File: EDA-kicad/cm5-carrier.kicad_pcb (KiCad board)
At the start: 2 copper layers, 82 x 154.8 mm, 94 parts, among them J1 SJ2-35894B-SMT-TR, J2 USBC-4-0-CX90MW9-24P1, J3 SIM-G85D1160022HHR, J4 FINGER, Q10 NMOS, Q3 NMOS, Q3_BAT1 NMOS, Q4 NMOS, Q4_BAT1 NMOS, Q5 NMOS, Q6 NMOS, Q7 NMOS, Q8 NMOS, Q9 NMOS, SW2 PROG, SW3 VOL-, SW4 VOL+, SW5 POW, SW6 CHP-041B, U1 EG25GGC-128-SGNS, U10 BAT-CONNECTOR-FLTS22WR00, U5 Flash-LED-Lumiled, U6 FPC15pin-1mm-pitch-F52Q-1A7H1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, U7 CODEC-TLV320AIC3204IRHBR, U8 DAC-TLV320DAC3100IRHBR, U9 GSM-GPS-EC25VFA-512-STD

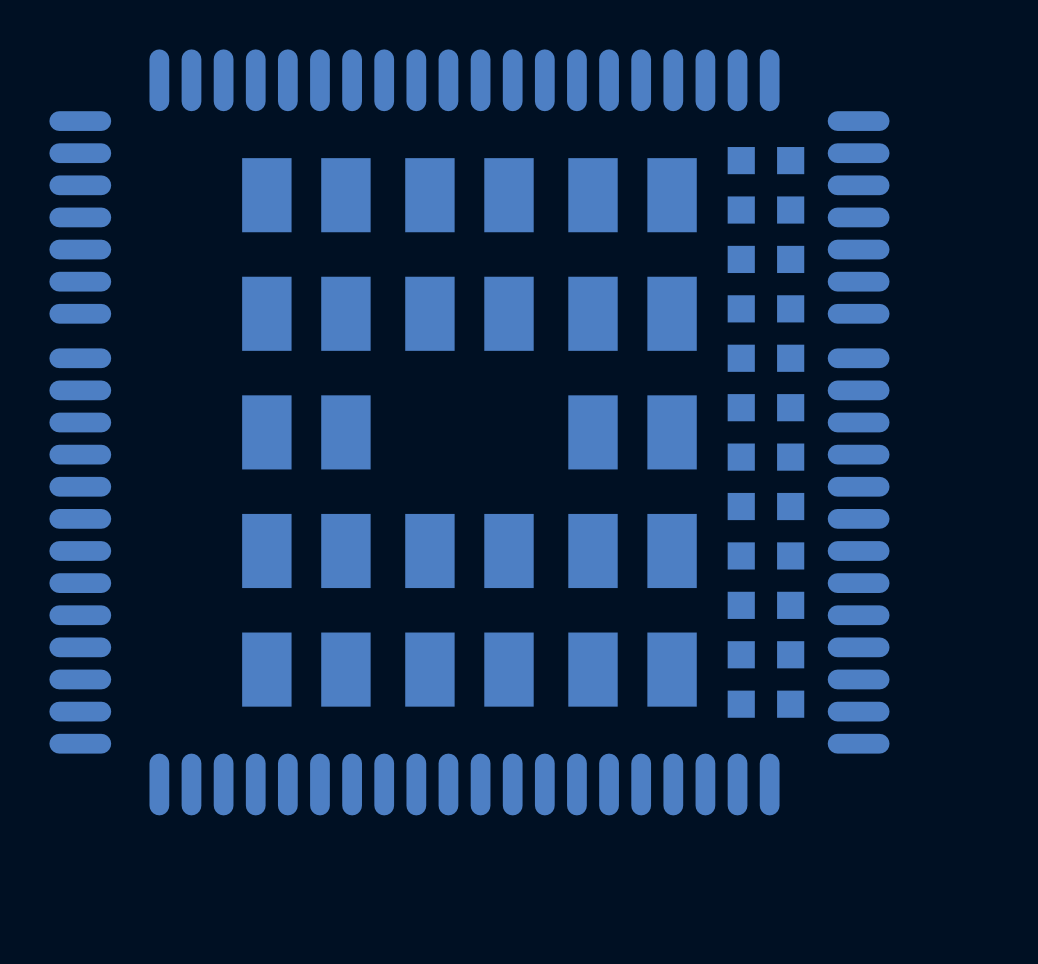
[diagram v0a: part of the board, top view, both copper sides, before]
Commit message: delete old ec25 footprint
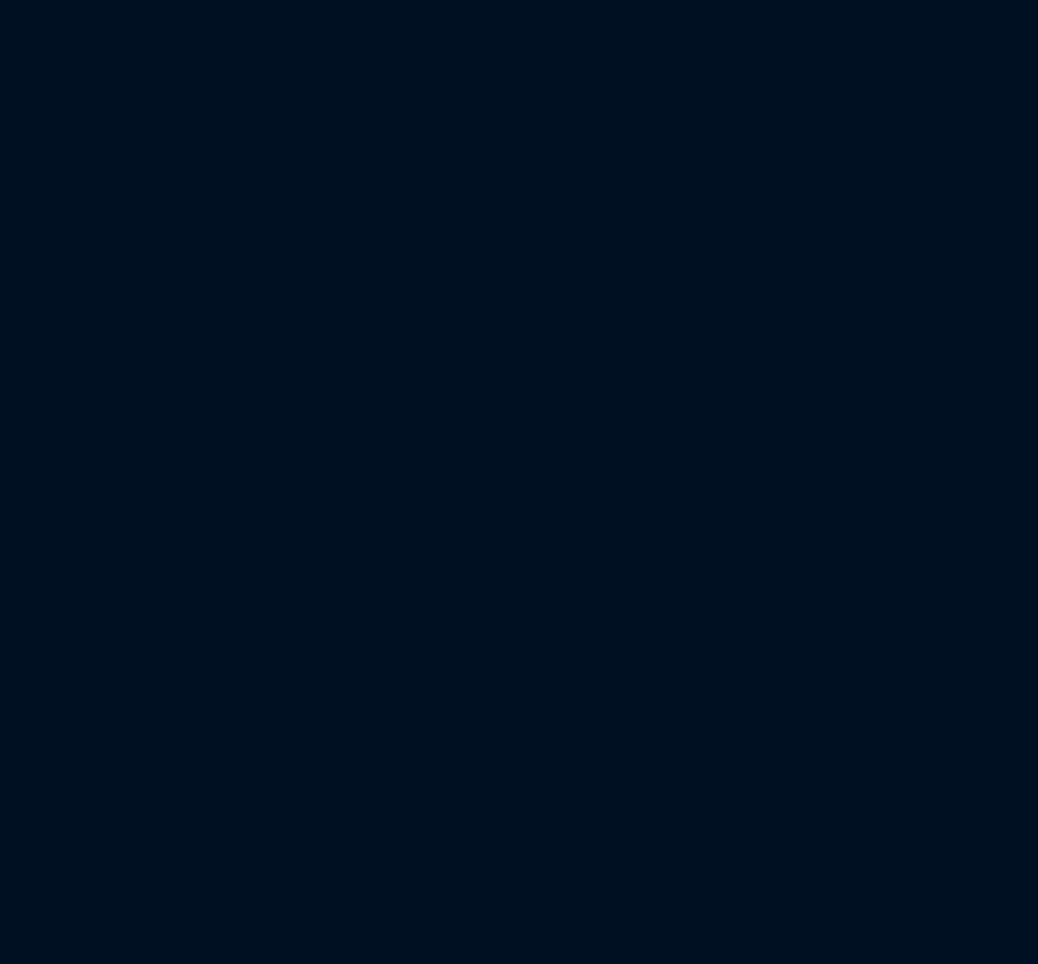
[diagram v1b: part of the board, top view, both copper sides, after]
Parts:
- removed U9: GSM-GPS-EC25VFA-512-STD, SPIRIT-footprints:GSM-GPS-XCVR_EC25VFA-512-STD

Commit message: set 6 layers, modify their settings
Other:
- copper layers 2 -> 6
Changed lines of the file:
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@@
 	(layers
 		(0 "F.Cu" signal)
+		(4 "In1.Cu" signal)
+		(6 "In2.Cu" signal)
+		(8 "In3.Cu" signal)
+		(10 "In4.Cu" signal)
 		(2 "B.Cu" signal)
 		(9 "F.Adhes" user "F.Adhesive")
@@
 	)
 	(setup
+		(stackup
+			(layer "F.SilkS"
+				(type "Top Silk Screen")
+			)
+			(layer "F.Paste"
+				(type "Top Solder Paste")
+			)
+			(layer "F.Mask"
+				(type "Top Solder Mask")
+				(thickness 0.01)
+			)
+			(layer "F.Cu"
+				(type "copper")
+				(thickness 0.035)
+			)
+			(layer "dielectric 1"
+				(type "prepreg")
+				(thickness 0.1)
+				(material "FR4")
+				(epsilon_r 4.5)
+				(loss_tangent 0.02)
+			)
+			(layer "In1.Cu"
+				(type "copper")
+				(thickness 0.035)
+			)
+			(layer "dielectric 2"
+				(type "core")
+				(thickness 0.535)
+				(material "FR4")
+				(epsilon_r 4.5)
+				(loss_tangent 0.02)
+			)
+			(layer "In2.Cu"
+				(type "copper")
+				(thickness 0.035)
+			)
+			(layer "dielectric 3"
+				(type "prepreg")
+				(thickness 0.1)
+				(material "FR4")
+				(epsilon_r 4.5)
+				(loss_tangent 0.02)
+			)
+			(layer "In3.Cu"
+				(type "copper")
+				(thickness 0.035)
+			)
+			(layer "dielectric 4"
+				(type "prepreg")
+				(thickness 0.535)
+				(material "FR4")
+				(epsilon_r 4.5)
+				(loss_tangent 0.02)
+			)
+			(layer "In4.Cu"
+				(type "copper")
+				(thickness 0.035)
+			)
+			(layer "dielectric 5"
+				(type "prepreg")
+				(thickness 0.1)
+				(material "FR4")
+				(epsilon_r 4.5)
+				(loss_tangent 0.02)
+			)
+			(layer "B.Cu"
+				(type "copper")
+				(thickness 0.035)
+			)
+			(layer "B.Mask"
+				(type "Bottom Solder Mask")
+				(thickness 0.01)
+			)
+			(layer "B.Paste"
+				(type "Bottom Solder Paste")
+			)
+			(layer "B.SilkS"
+				(type "Bottom Silk Screen")
+			)
+			(copper_finish "None")
+			(dielectric_constraints no)
+		)
 		(pad_to_mask_clearance 0)
 		(allow_soldermask_bridges_in_footprints no)

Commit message: add monkeys
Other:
- board text added: "Design by a thousand of monkey with Kicad"
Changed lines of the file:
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@@
+		)
+	)
+	(gr_text "Design by a thousand of monkey with Kicad"
+		(at 50 27 0)
+		(layer "F.Cu")
+		(effects
+			(font
+				(size 1.27 1.27)
+			)
 		)
 	)

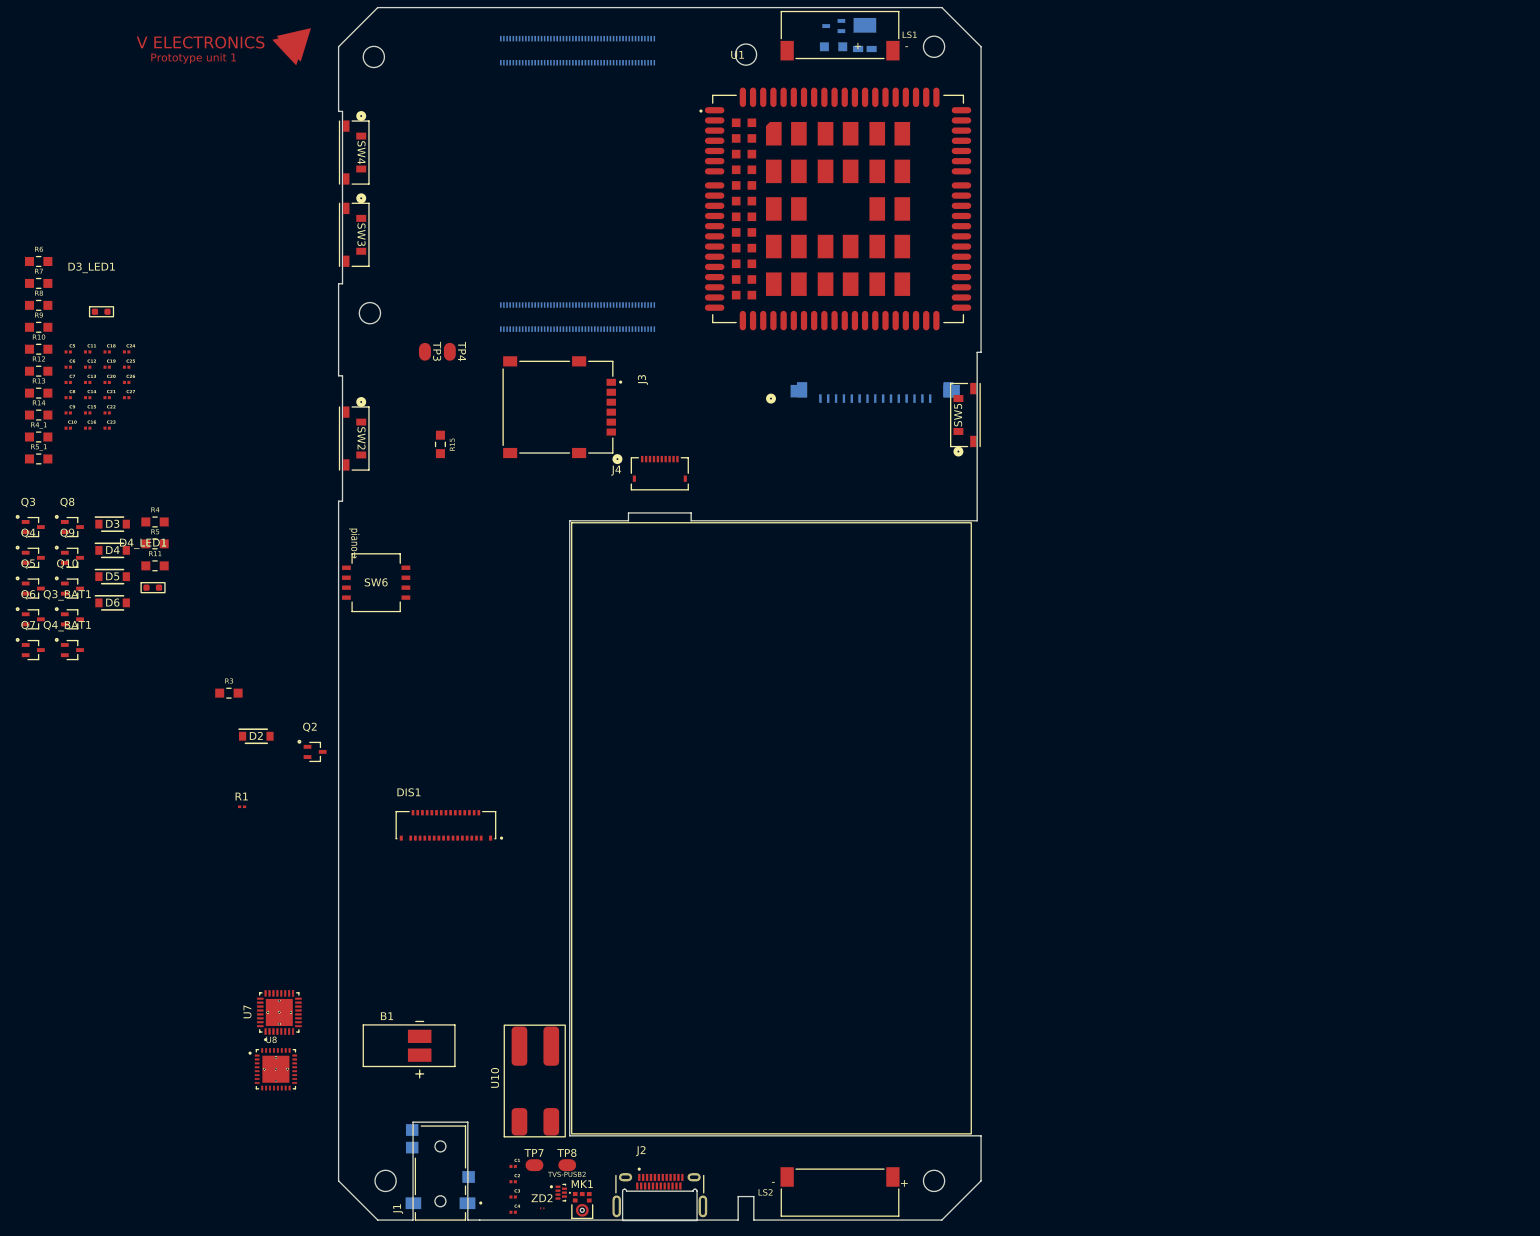
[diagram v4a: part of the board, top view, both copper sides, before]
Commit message: assign power section footprints and import to pcb
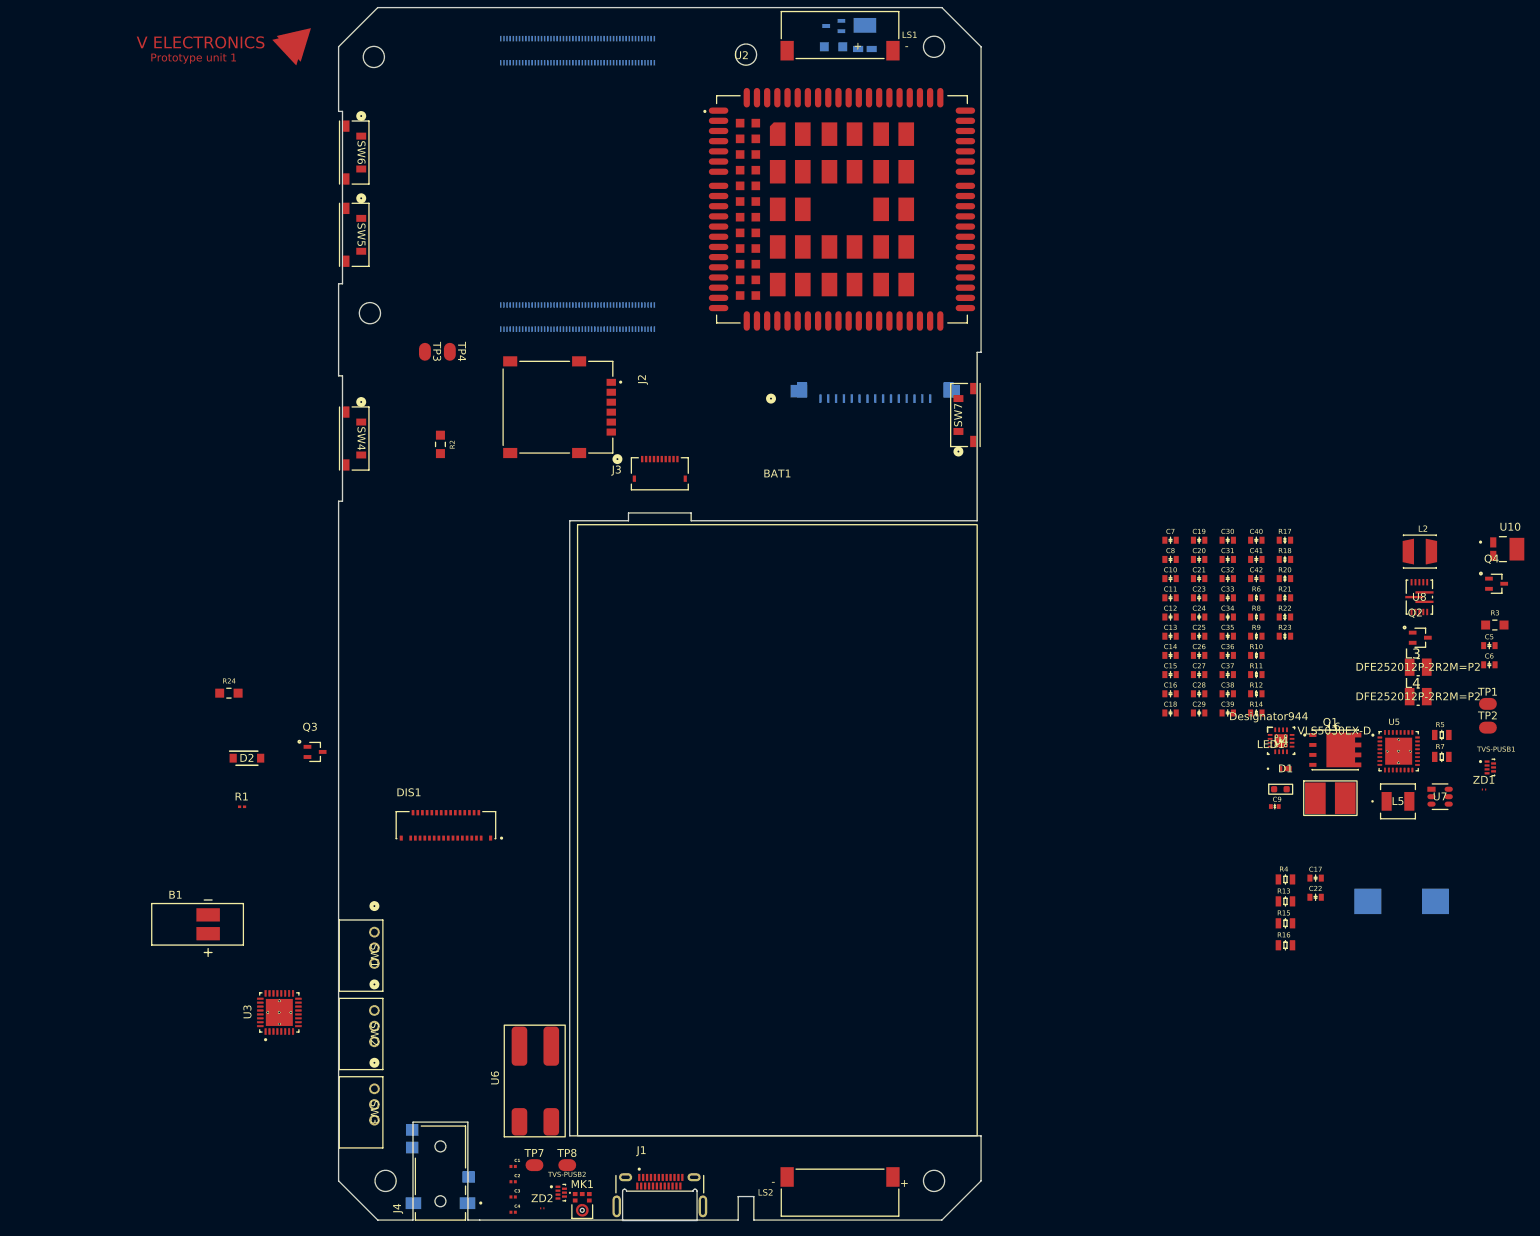
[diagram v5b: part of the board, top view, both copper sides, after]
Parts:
- removed BAT2: battery_37V3500mAhLP685077JU, SPIRIT-footprints:battery_37V3500mAhLP685077JU
- removed D3, D4, D5, D6: D, SPIRIT-footprints:flyback-diode-SODFL3818X130N
- removed D3_LED1: LED-INDICATOR, SPIRIT-footprints:LED-INDICATOR
- removed D4_LED1: LED, SPIRIT-footprints:LED-INDICATOR
- removed Q10, Q3_BAT1, Q4_BAT1, Q5, Q6, Q7, Q8, Q9: NMOS, SPIRIT-footprints:gpio-driver-transistor-fix-SOT65P210X110-3N
- removed the Q3 at (15.0, 97.3)
- removed R4_1: 6.04k, SPIRIT-footprints:1K-05W-0805-RES_ERJP06J102V
- removed R5_1: 100k, SPIRIT-footprints:1K-05W-0805-RES_ERJP06J102V
- removed the SW6 at (58.8, 104.4)
- removed U1: EG25GGC-128-SGNS, SPIRIT-footprints:XCVR_EG25GGC-128-SGNS
- added BAT1: Li-ion-3.7 35Ah, SPIRIT-footprints:battery_37V3500mAhLP685077JU, F.Cu at (110.0, 102.0)
- added C17: 0.1μF, SPIRIT-footprints:0603-capacitor, F.Cu at (178.7, 142.1)
- added C28: 10μF, SPIRIT-footprints:0603-capacitor, F.Cu at (163.8, 118.6)
- added C29: 10μF, SPIRIT-footprints:0603-capacitor, F.Cu at (163.8, 121.0)
- added C30: 1μF, SPIRIT-footprints:0603-capacitor, F.Cu at (167.5, 99.0)
- added C31: 1μF, SPIRIT-footprints:0603-capacitor, F.Cu at (167.5, 101.4)
- added C32: 0.1μF, SPIRIT-footprints:0603-capacitor, F.Cu at (167.5, 103.9)
- added C33: 22μF, SPIRIT-footprints:0603-capacitor, F.Cu at (167.5, 106.3)
- added C34: 22μF, SPIRIT-footprints:0603-capacitor, F.Cu at (167.5, 108.8)
- added C35: 22μF, SPIRIT-footprints:0603-capacitor, F.Cu at (167.5, 111.2)
- added C36: 0.1μF, SPIRIT-footprints:0603-capacitor, F.Cu at (167.5, 113.7)
- added C37: 22μF, SPIRIT-footprints:0603-capacitor, F.Cu at (167.5, 116.1)
- added C38: 22μF, SPIRIT-footprints:0603-capacitor, F.Cu at (167.5, 118.6)
- added C39: 22μF, SPIRIT-footprints:0603-capacitor, F.Cu at (167.5, 121.0)
- added C40: 6.8nF, SPIRIT-footprints:0603-capacitor, F.Cu at (171.1, 99.0)
- added C41: 4.7μF, SPIRIT-footprints:0603-capacitor, F.Cu at (171.1, 101.4)
- added C42: 22μF, SPIRIT-footprints:0603-capacitor, F.Cu at (171.1, 103.9)
- added D1: D_Schottky, SPIRIT-footprints:schottky-diode-CR_DSN2_152AB-C_OSI, F.Cu at (174.9, 128.1)
- added L1: 2.2uH, SPIRIT-footprints:2-2uh-inductorIND_ETQP4M2R2KVC, B.Cu at (189.7, 145.1)
- added L2: 3.3uH, SPIRIT-footprints:3-3uH-MURATA_LQH44PN3R3MPRL, F.Cu at (192.0, 100.4)
- added L3: 2.2uH, SPIRIT-footprints:2-2uH-inductor-INDC2520X120N, F.Cu at (191.8, 115.2)
- added L4: 2.2uH, SPIRIT-footprints:2-2uH-inductor-INDC2520X120N, F.Cu at (191.8, 118.9)
- added L5: 6.8uH, SPIRIT-footprints:6-8uH-inductor-LQH44PN6R8MPRLIND_LQH44PN_PR_MUR, F.Cu at (189.2, 132.3)
- added L6: 1.5uH, SPIRIT-footprints:1-5uH-inductor-VLS5030EX-D, F.Cu at (180.6, 129.8)
- added LED1: 5mA 2V Fv, SPIRIT-footprints:LED-INDICATOR-RED-QBLP601-R5, F.Cu at (172.7, 130.1)
- added Q1: ~, SPIRIT-footprints:NMOS-BSC0902NSIATMA1-PG-TDSON-8-6-IC_ISC037N03L5ISATMA1, F.Cu at (181.2, 125.7)
- added Q2: ~, SPIRIT-footprints:gpio-driver-transistor-fix-SOT65P210X110-3N, F.Cu at (192.1, 111.4)
- added R15: 10k, SPIRIT-footprints:0805-resistor, F.Cu at (174.8, 147.9)
- added R16: 30k, SPIRIT-footprints:0805-resistor, F.Cu at (174.8, 150.7)
- added R17: 680, SPIRIT-footprints:0603-resistor, F.Cu at (174.8, 99.0)
- added R18: 10k, SPIRIT-footprints:0603-resistor, F.Cu at (174.8, 101.4)
- added R20: 5, SPIRIT-footprints:0603-resistor, F.Cu at (174.8, 103.9)
- added R21: 750k, SPIRIT-footprints:0603-resistor, F.Cu at (174.8, 106.3)
- added R22: 200k, SPIRIT-footprints:0603-resistor, F.Cu at (174.8, 108.8)
- added R23: 6.8k, SPIRIT-footprints:0603-resistor, F.Cu at (174.8, 111.2)
- added R3: 100K-0805-resistor-ERA6AEB104V, SPIRIT-footprints:100K-0805-resistor-RES_ERA6AEB104V, F.Cu at (201.6, 109.8)
- added SW1: EG25-switch-CSS-1210MC, SPIRIT-footprints:privacy-switch-SW3_CSS-1210MC_NDC, F.Cu at (58.6, 149.0)
- added SW2: MIC-switch-CSS-1210MC, SPIRIT-footprints:privacy-switch-SW3_CSS-1210MC_NDC, F.Cu at (58.6, 159.0)
- added SW3: CAM-switch-CSS-1210MC, SPIRIT-footprints:privacy-switch-SW3_CSS-1210MC_NDC, F.Cu at (58.6, 169.0)
- added TP1: test-pad-1, SPIRIT-footprints:test-pad-1, F.Cu at (200.7, 118.9)
- added TP2: test-pad-1, SPIRIT-footprints:test-pad-1, F.Cu at (200.7, 121.9)
- added TVS-PUSB1: ~, SPIRIT-footprints:TVS-array-IC_PUSB3AB6Z, F.Cu at (201.0, 128.0)
- added U10: Flash-LED-Lumiled, SPIRIT-footprints:LUMILED-DIODFN449X305X210-3N, F.Cu at (203.2, 100.1)
- added U2: EG25GGC-128-SGNS, SPIRIT-footprints:XCVR_EG25GGC-128-SGNS, F.Cu at (118.2, 56.8)
- added U4: BQ25792RQMR, SPIRIT-footprints:CHARGER-SWITCHER-RTE0016C, F.Cu at (174.3, 124.6)
- added U5: TPS650250RHBR, SPIRIT-footprints:TPS650250-IC_ADS125H01IRHBT, F.Cu at (189.3, 125.9)
- added U7: 22V-boost-AP3032KTR-G1, SPIRIT-footprints:SOT23-6_DIO, F.Cu at (194.6, 131.7)
- added ZD1: protection-PESD5V0C1USFYL, SPIRIT-footprints:USB-ESD-protection-diode-PESD5V0C1USFYL-SOD962-2_DSN0603-2_NEX, F.Cu at (200.2, 130.8)
- C10: value 10μF -> 4.7μF; footprint SPIRIT-footprints:USBC_capacitor_CAPC0603X33N -> SPIRIT-footprints:0603-capacitor
- C11, C12, C13, C14, C22, C7, C8: footprint SPIRIT-footprints:USBC_capacitor_CAPC0603X33N -> SPIRIT-footprints:0603-capacitor
- C15, C16: value 10μF -> 47nF; footprint SPIRIT-footprints:USBC_capacitor_CAPC0603X33N -> SPIRIT-footprints:0603-capacitor
- C18, C19: value 47nF -> 10μF; footprint SPIRIT-footprints:USBC_capacitor_CAPC0603X33N -> SPIRIT-footprints:0603-capacitor
- C20: value 4.7μF -> 10μF; footprint SPIRIT-footprints:USBC_capacitor_CAPC0603X33N -> SPIRIT-footprints:0603-capacitor
- C21, C24, C27: value 0.1μF -> 10μF; footprint SPIRIT-footprints:USBC_capacitor_CAPC0603X33N -> SPIRIT-footprints:0603-capacitor
- C23: value 10μF -> 1μF; footprint SPIRIT-footprints:USBC_capacitor_CAPC0603X33N -> SPIRIT-footprints:0603-capacitor
- C25, C26: value 2.2μF -> 10μF; footprint SPIRIT-footprints:USBC_capacitor_CAPC0603X33N -> SPIRIT-footprints:0603-capacitor
- C5: value 0.1μF -> 200-pf-CC0603KRX7R7BB104; footprint SPIRIT-footprints:USBC_capacitor_CAPC0603X33N -> SPIRIT-footprints:0603-capacitor
- C6: value 10μF -> 01-uf-CC0603KRX7R7BB104; footprint SPIRIT-footprints:USBC_capacitor_CAPC0603X33N -> SPIRIT-footprints:0603-capacitor
- C9: value 10μF -> 1nF 50V; footprint SPIRIT-footprints:USBC_capacitor_CAPC0603X33N -> SPIRIT-footprints:0402-capacitor
- Q4: value NMOS -> ~
- R10: value R -> 182K; footprint SPIRIT-footprints:1K-05W-0805-RES_ERJP06J102V -> SPIRIT-footprints:0603-resistor
- R11: value R -> 1M; footprint SPIRIT-footprints:1K-05W-0805-RES_ERJP06J102V -> SPIRIT-footprints:0603-resistor
- R12: value R -> 470k; footprint SPIRIT-footprints:1K-05W-0805-RES_ERJP06J102V -> SPIRIT-footprints:0603-resistor
- R13: value 2 -> 5.23k; footprint SPIRIT-footprints:1K-05W-0805-RES_ERJP06J102V -> SPIRIT-footprints:0805-resistor
- R14: value 2 -> 10k; footprint SPIRIT-footprints:1K-05W-0805-RES_ERJP06J102V -> SPIRIT-footprints:0603-resistor
- R4: footprint SPIRIT-footprints:1K-05W-0805-RES_ERJP06J102V -> SPIRIT-footprints:0805-resistor
- R5: value 2.2k -> 4.7K; footprint SPIRIT-footprints:1K-05W-0805-RES_ERJP06J102V -> SPIRIT-footprints:0805-resistor
- R6: value 5.24k -> 820k; footprint SPIRIT-footprints:1K-05W-0805-RES_ERJP06J102V -> SPIRIT-footprints:0603-resistor
- R7: value 30.31k -> 100k; footprint SPIRIT-footprints:1K-05W-0805-RES_ERJP06J102V -> SPIRIT-footprints:0805-resistor
- R8: value 10k -> 47k; footprint SPIRIT-footprints:1K-05W-0805-RES_ERJP06J102V -> SPIRIT-footprints:0603-resistor
- R9: footprint SPIRIT-footprints:1K-05W-0805-RES_ERJP06J102V -> SPIRIT-footprints:0603-resistor
- U8: value DAC-TLV320DAC3100IRHBR -> MP3429GL-Z; footprint SPIRIT-footprints:DAC-IC_ADS125H01IRHBT -> SPIRIT-footprints:QFN-3x4_MP3429_MNP
- moved R7 189.0 mm to (194.8, 126.6)
- moved Q4 186.8 mm to (201.8, 104.5)
- moved C6 185.3 mm to (200.9, 114.9)
- moved C5 185.2 mm to (200.9, 112.4)
- moved R13 171.8 mm to (174.8, 145.1)
- moved C22 166.2 mm to (178.7, 144.6)
- moved R5 166.0 mm to (194.8, 123.8)
- moved C9 162.0 mm to (173.5, 133.0)
- moved R6 161.2 mm to (171.1, 106.3)
- moved R12 160.8 mm to (171.1, 118.6)
- moved R8 160.4 mm to (171.1, 108.8)
- moved R9 160.3 mm to (171.1, 111.2)
- moved R10 160.2 mm to (171.1, 113.7)
- moved R14 160.0 mm to (171.1, 121.0)
- moved U8 157.9 mm to (191.9, 106.2)
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- renumbered J2 to J1, J3 to J2, J4 to J3, J1 to J4, Q2 to Q3, Q1 to Q4, R15 to R2, R3 to R24, R2 to R25, SW2 to SW4, SW3 to SW5, SW4 to SW6, SW5 to SW7, U5 to U10, U7 to U3, U10 to U6, U6 to U9
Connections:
- net CODEC SCL renamed AUDIO_SCL
- net CODEC SDA renamed AUDIO_SDA
- C10 pad 1: SYS -> REGN
- C15 pad 1: BAT -> Net-(U4-SW1)
- C15 pad 2: GND -> Net-(U4-BTST1)
- C16 pad 1: BAT -> Net-(U4-SW2)
- C16 pad 2: GND -> Net-(U4-BTST2)
- C18 pad 1: BTST1 -> SYS
- C18 pad 2: REGN -> GND
- C19 pad 1: REGN -> SYS
- C19 pad 2: BTST2 -> GND
- C20 pad 1: REGN -> SYS
- C21 pad 1: VBUS -> SYS
- C22 pad 1: VBUS -> SYS
- C23 pad 1: VBUS -> SYS
- C24 pad 1: VAC2 -> SYS
- C25 pad 1: Net-(C25-Pad1) -> SYS
- C26 pad 1: Net-(C26-Pad1) -> SYS
- C27 pad 1: VAC1 -> 3V3A
- C5 pad 1: SYS -> GND
- C5 pad 2: GND -> MIC-SWITCH
- C6 pad 1: SYS -> MIC-SWITCH
- C7 pad 1: SYS -> BAT+
- C8 pad 1: SYS -> BAT+
- C9 pad 1: SYS -> Net-(U4-SDRV)
- MK1 pad 1: unconnected-(MK1-WS-Pad1) -> AUDIO_WCLK_I2S
- MK1 pad 2: unconnected-(MK1-SELECT-Pad2) -> GND
- MK1 pad 4: unconnected-(MK1-BCLK-Pad4) -> AUDIO_BCLK_I2S
- MK1 pad 6: unconnected-(MK1-DATA_OUT-Pad6) -> AUDIO_MIC_DATA
- Module1 pad 26: unconnected-(Module1A-GPIO19-Pad26) -> AUDIO_WCLK_I2S
- Module1 pad 27: unconnected-(Module1A-GPIO20-Pad27) -> AUDIO_MIC_DATA
- Module1 pad 30: DIS SDA -> DIS_SDA
- Module1 pad 37: DIS SCL -> DIS_SCL
- Module1 pad 41: unconnected-(Module1A-GPIO25-Pad41) -> AUDIO_MCLK
- Module1 pad 49: unconnected-(Module1A-GPIO18-Pad49) -> AUDIO_BCLK_I2S
- Module1 pad 55: unconnected-(Module1A-GPIO14-Pad55) -> LCD_PWM
- Q4 pad 1: OUT + -> Net-(Q4-G)
- Q4 pad 2: SDRV -> Net-(Q4-D)
- Q4 pad 3: BAT -> GND
- Q4 pad 1: Net-(Q1-G) -> Net-(Q4-G)
- Q4 pad 2: Net-(Q1-D) -> Net-(Q4-D)
- R10 pad 1: VBUS -> GND
- R10 pad 2: PMID -> Net-(U5-DEFDCDC3)
- R11 pad 1: Net-(D5-K) -> Net-(U5-PWRFAIL_SNS)
- R11 pad 2: ACDRV1 -> SYS
- R12 pad 1: Net-(D6-K) -> GND
- R12 pad 2: ACDRV2 -> Net-(U5-PWRFAIL_SNS)
- R13 pad 1: Net-(C25-Pad1) -> REGN
- R13 pad 2: VAC2 -> Net-(U4-TS)
- R14 pad 1: Net-(C26-Pad1) -> Net-(LED1-K)
- R14 pad 2: VAC1 -> VCC
- R25 pad 2: Net-(Q1-G) -> Net-(Q4-G)
- R4 pad 1: ILIM_HIZ -> Net-(U4-ILIM_HIZ)
- R5 pad 1: Net-(D4_LED1-A) -> GND
- R5 pad 2: REGN -> Net-(U4-PROG)
- R6 pad 1: REGN -> 3V3B
- R6 pad 2: Net-(U11-TS) -> Net-(U5-DEFDCDC3)
- R7 pad 1: Net-(U11-TS) -> Net-(U4-ILIM_HIZ)
- R8 pad 1: Net-(U11-TS) -> 3V3
- R8 pad 2: GND -> ~{PWRFAIL}
- R9 pad 1: BATP -> Net-(U4-BATP)
- R9 pad 2: OUT + -> BAT+
- U10 pad 1: Net-(Q1-D) -> Net-(Q4-D)
- U3 pad 1: unconnected-(U7-MCLK-Pad1) -> AUDIO_MCLK
- U3 pad 2: unconnected-(U7-BCLK-Pad2) -> AUDIO_BCLK_I2S
- U3 pad 3: unconnected-(U7-WCLK-Pad3) -> AUDIO_WCLK_I2S
- U6 pad 3: OUT + -> BAT+
- U8 pad 1: GND -> Net-(U8-SW)
- U8 pad 10: unconnected-(U8-SCL-Pad10) -> SYS
- U8 pad 11: unconnected-(U8-VOL/MICDET-Pad11) -> SYS
- U8 pad 12: unconnected-(U8-MICBIAS-Pad12) -> SYS
- U8 pad 13: unconnected-(U8-AIN1-Pad13) -> Net-(U8-BST)
- U8 pad 2: VCC -> Net-(U8-VDD)
- U8 pad 3: VCC -> Net-(U8-SS)
- U8 pad 4: (no net) -> Net-(U8-COMP)
- U8 pad 5: unconnected-(U8-DIN-Pad5) -> Net-(U8-FB)
- U8 pad 6: unconnected-(U8-WCLK-Pad6) -> AGND
- U8 pad 7: unconnected-(U8-BCLK-Pad7) -> GND
- U8 pad 8: unconnected-(U8-MCLK-Pad8) -> 5V
- U8 pad 9: unconnected-(U8-SDA-Pad9) -> AGND
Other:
- board text removed: "piano→"
